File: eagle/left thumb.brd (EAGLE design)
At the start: 41.9 x 42.5 mm, 12 parts, among them J1 B7B-ZR_(LF)(SN)

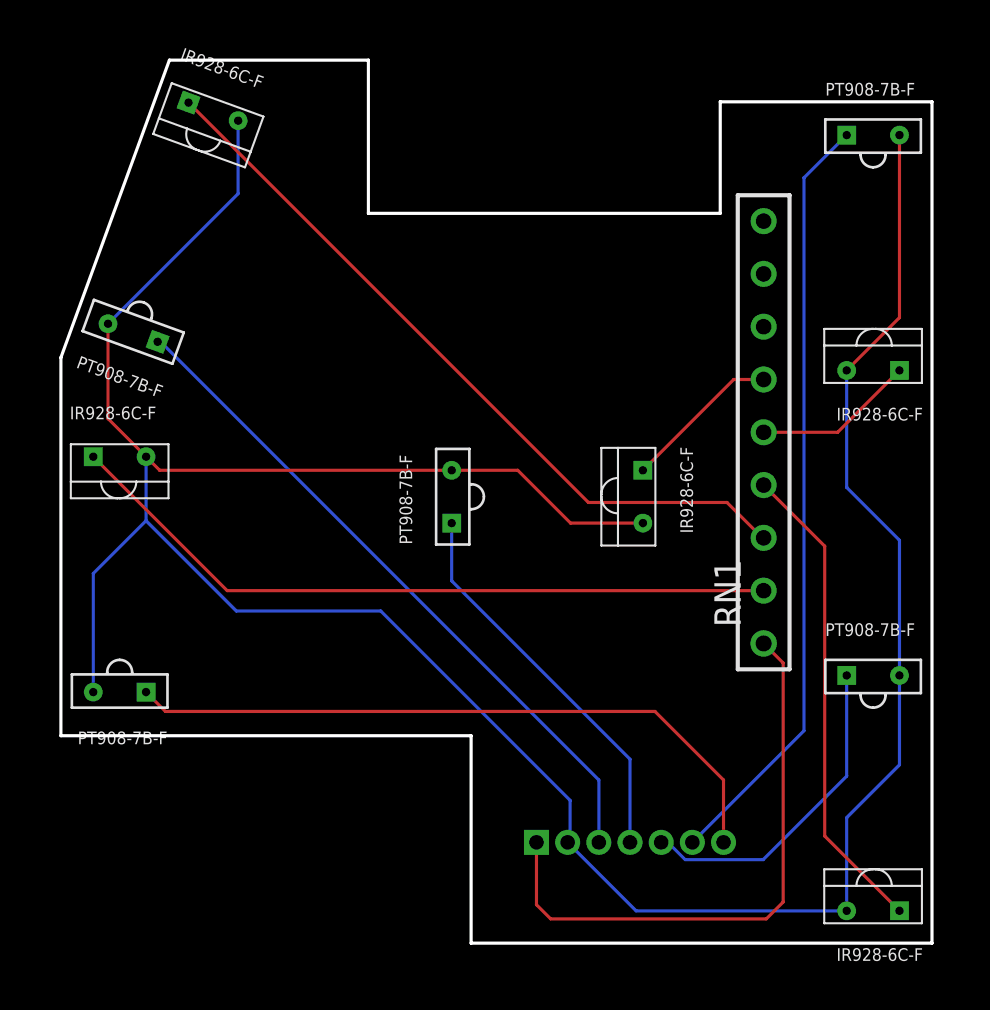
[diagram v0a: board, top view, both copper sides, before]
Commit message: Fix drill holes and outer dimensions on cluster and left thumb cluster
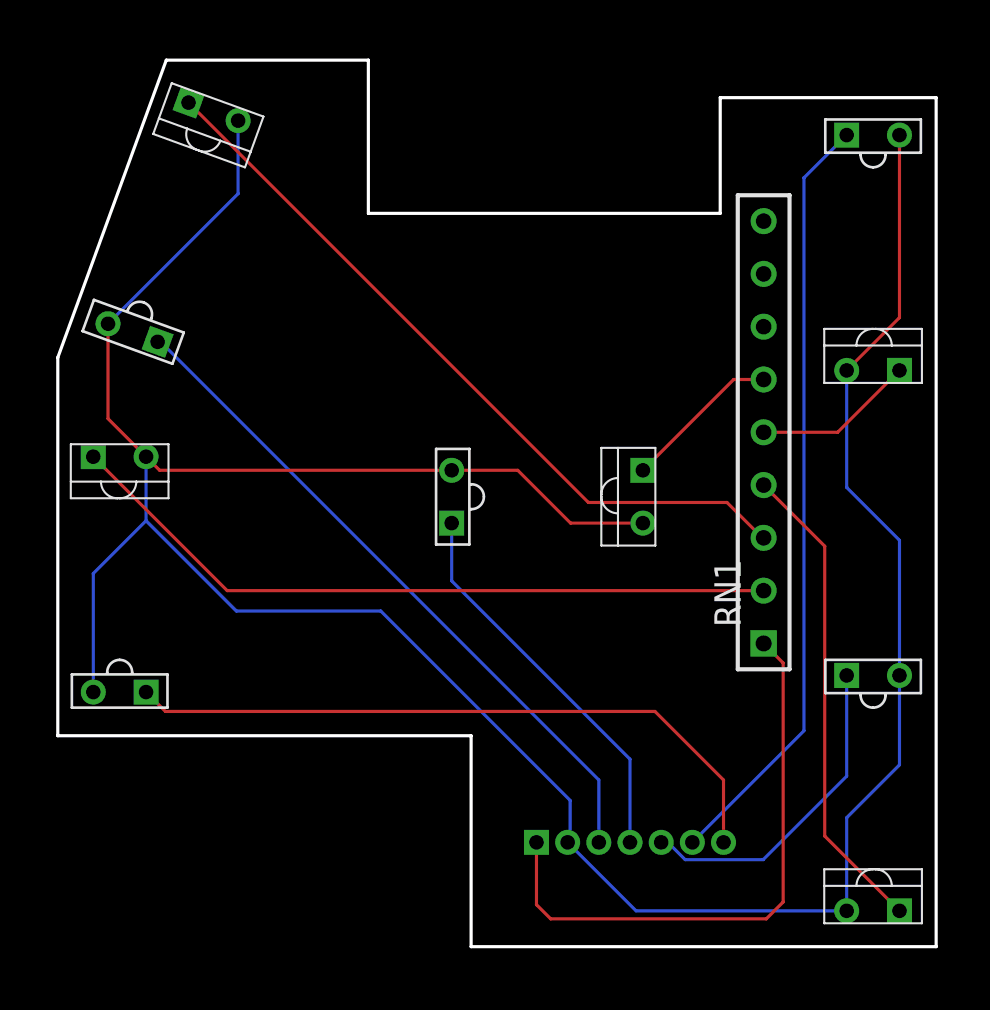
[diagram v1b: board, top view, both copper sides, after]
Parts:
- RN1: value 4309R-101-202LF -> 150R; device 4309R-101-202LF:4309R-101 -> 9 pin resistor network:9PIN-RESISTOR-NETWORK
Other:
- board size 41.9 x 42.5 mm -> 42.3 x 42.7 mm
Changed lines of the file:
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@@
 <?xml version="1.0" encoding="utf-8"?>
 <!DOCTYPE eagle SYSTEM "eagle.dtd">
-<eagle version="9.3.2">
+<eagle version="9.4.2">
 <drawing>
 <settings>
@@
 <setting verticaltext="up"/>
 </settings>
-<grid distance="1" unitdist="mm" unit="mm" style="lines" multiple="1" display="no" altdistance="0.01" altunitdist="mm" altunit="mm"/>
+<grid distance="0.1" unitdist="mm" unit="mm" style="lines" multiple="1" display="no" altdistance="0.01" altunitdist="mm" altunit="mm"/>
 <layers>
 <layer number="1" name="Top" color="4" fill="1" visible="yes" active="yes"/>
@@
 <board>
 <plain>
-<wire x1="0.248309375" y1="29.195" x2="0.248309375" y2="10.9998" width="0.1524" layer="20"/>
-<wire x1="0.248309375" y1="10.9998" x2="19.9849" y2="10.9998" width="0.1524" layer="20"/>
-<wire x1="19.9849" y1="10.9998" x2="19.9849" y2="1.02" width="0.1524" layer="20"/>
-<wire x1="19.9849" y1="1.02" x2="42.16" y2="1.02" width="0.1524" layer="20"/>
-<wire x1="42.16" y1="1.02" x2="42.16" y2="41.5" width="0.1524" layer="20"/>
-<wire x1="42.16" y1="41.5" x2="31.9711" y2="41.5" width="0.1524" layer="20"/>
-<wire x1="31.9711" y1="41.5" x2="31.9711" y2="36.1334" width="0.1524" layer="20"/>
+<wire x1="0.098309375" y1="29.195" x2="0.098309375" y2="10.9998" width="0.1524" layer="20"/>
+<wire x1="0.098309375" y1="10.9998" x2="19.9849" y2="10.9998" width="0.1524" layer="20"/>
+<wire x1="19.9849" y1="10.9998" x2="19.9849" y2="0.85" width="0.1524" layer="20"/>
+<wire x1="19.9849" y1="0.85" x2="42.36" y2="0.85" width="0.1524" layer="20"/>
+<wire x1="42.36" y1="0.85" x2="42.36" y2="41.7" width="0.1524" layer="20"/>
+<wire x1="42.36" y1="41.7" x2="31.9711" y2="41.7" width="0.1524" layer="20"/>
+<wire x1="31.9711" y1="41.7" x2="31.9711" y2="36.1334" width="0.1524" layer="20"/>
 <wire x1="31.9711" y1="36.1334" x2="15.0421" y2="36.1334" width="0.1524" layer="20"/>
 <wire x1="15.0421" y1="36.1334" x2="15.0421" y2="43.5054" width="0.1524" layer="20"/>
-<wire x1="15.0421" y1="43.5054" x2="5.468390625" y2="43.5054" width="0.1524" layer="20"/>
-<wire x1="5.468390625" y1="43.5054" x2="0.248309375" y2="29.195" width="0.1524" layer="20"/>
+<wire x1="15.0421" y1="43.5054" x2="5.318390625" y2="43.5054" width="0.1524" layer="20"/>
+<wire x1="5.318390625" y1="43.5054" x2="0.098309375" y2="29.195" width="0.1524" layer="20"/>
 </plain>
 <attributes>
@@
 <attribute name="VALUE" x="5.595884375" y="28.848196875" size="1.016" layer="27" rot="R160"/>
 </element>
-<element name="RN1" library="4309R-101-202LF" package="4309R-101" value="4309R-101-202LF" x="34.06" y="15.44" smashed="yes" rot="R90">
-<attribute name="DESCRIPTION" value="Resistor Networks &amp; Arrays 9pin 2Kohms Bussed Low Profile" x="36" y="51" size="1.778" layer="27" rot="R90" display="off"/>
+<element name="RN1" library="9 pin resistor network" package="9PIN-RESISTOR-NETWORK" value="150R" x="34.06" y="15.44" smashed="yes" rot="R90">
 <attribute name="HEIGHT" value="mm" x="36" y="51" size="1.778" layer="27" rot="R90" display="off"/>
-<attribute name="MANUFACTURER_NAME" value="Bourns" x="36" y="51" size="1.778" layer="27" rot="R90" display="off"/>
-<attribute name="MANUFACTURER_PART_NUMBER" value="4309R-101-202LF" x="36" y="51" size="1.778" layer="27" rot="R90" display="off"/>
-<attribute name="MOUSER_PART_NUMBER" value="652-4309R-1LF-2K" x="36" y="51" size="1.778" layer="27" rot="R90" display="off"/>
-<attribute name="MOUSER_PRICE-STOCK" value="https://www.mouser.com/Search/Refine.aspx?Keyword=652-4309R-1LF-2K" x="36" y="51" size="1.778" layer="27" rot="R90" display="off"/>
 <attribute name="NAME" x="32.32233125" y="17.85966875" size="1.27" layer="25" rot="R90" align="center"/>
 <attribute name="VALUE" x="32.32233125" y="29.85966875" size="1.27" layer="27" rot="R90" align="center"/>

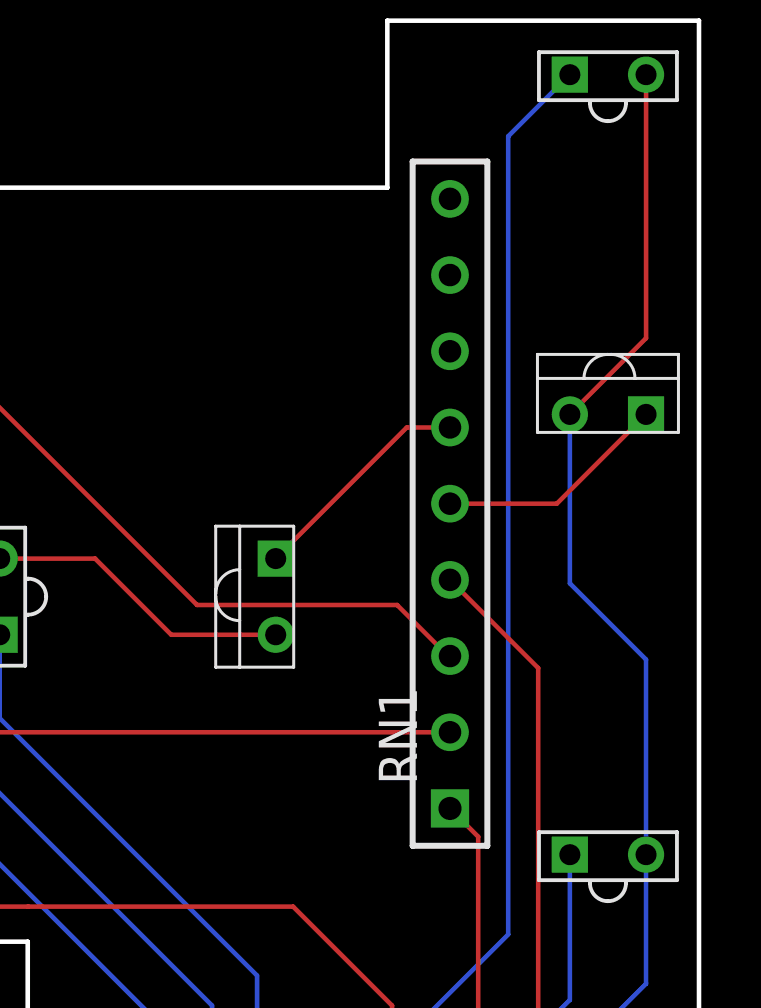
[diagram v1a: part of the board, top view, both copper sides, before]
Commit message: Reduce drill size of resistor holes. Fix right thumb cluster
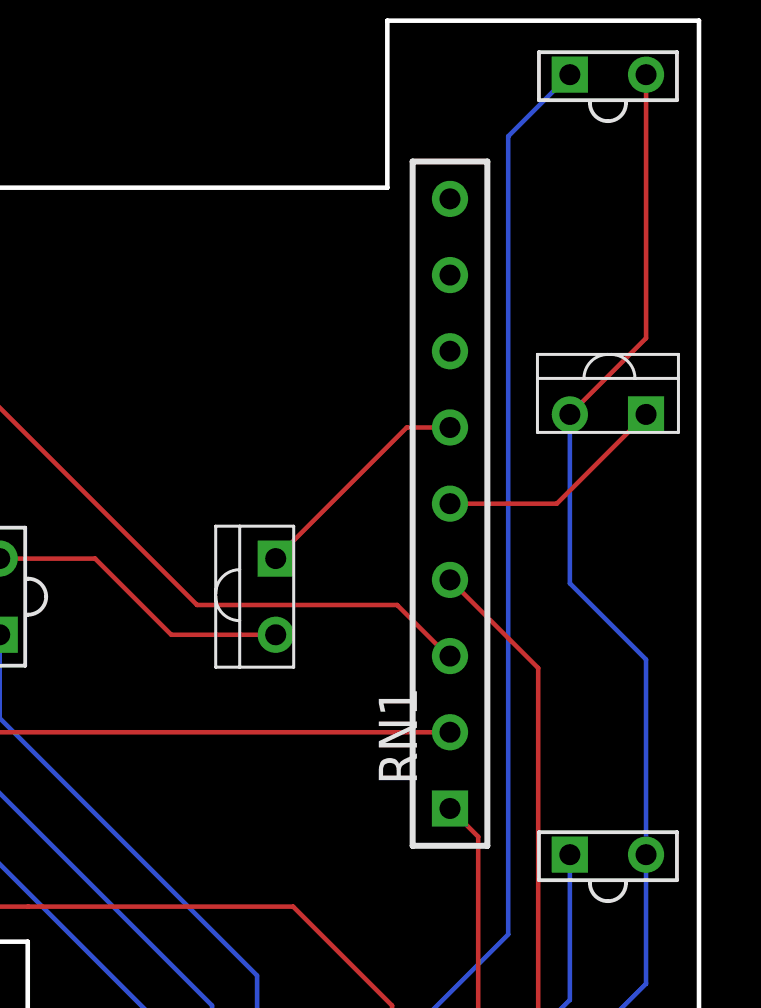
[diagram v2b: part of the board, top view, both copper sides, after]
